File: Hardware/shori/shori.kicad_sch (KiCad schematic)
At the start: 100 parts, among them J1 430450200, J2 SWD_Header, J3 UART_Header, J4 530480310, J5 AudioJack3, J6 530480210, U1 CS4272, U2 STM32H750VBTx, U3 NE5532, U4 NE5532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

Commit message: Routing and memes done!!
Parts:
- removed J5: AudioJack3, Connector_Audio:Jack_3.5mm_CUI_SJ1-3523N_Horizontal, symbol Connector_Audio:AudioJack3
- removed U6: OPA134, Package_TO_SOT_SMD:SOT-23-5_HandSoldering, symbol Amplifier_Operational:OPA134
- added J5: Conn_01x03, Connector_JST:JST_PH_S3B-PH-K_1x03_P2.00mm_Horizontal, symbol Connector_Generic:Conn_01x03
- added J7: 530480210, My footprints:CONN02_530480210_MOL, symbol 2 Pin Audio Molex:530480210
- added U7: TLV9001IDCK, Package_TO_SOT_SMD:SOT-353_SC-70-5, symbol Amplifier_Operational:TLV9001IDCK
- H1, H2, H3, H4: footprint MountingHole:MountingHole_3mm -> MountingHole:MountingHole_3.5mm
- J1: footprint MyFootprints:CONN_SD-43045-001_02_MOL -> Connector_JST:JST_XH_S2B-XH-A_1x02_P2.50mm_Horizontal
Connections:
- net +5V: now also J7.2
- net +5VA: now also U7.5 (V+)
- net AUDIO_OUT: now also J6.1; no longer J6.2
- net GND: now also J6.2, J5.2 (Pin_2), J7.1, U7.2 (V-); no longer J6.1
- net JACKR: now also J5.1 (Pin_1)
- net JACKT: now also J5.3 (Pin_3)
- net SWCLK: now also J2.2 (Pin_2); no longer J2.3 (Pin_3)
- net SWDIO: now also J2.3 (Pin_3); no longer J2.2 (Pin_2)
- net at C43.1, C45.2, R28.2: now also U7.4
- net FEEDBACK_CAP: now reaches C45.1, R27.2
- net FEEDBACK_CAP: now also U7.3 (-)
- net at C44.1, R24.2: now also U7.1 (+)
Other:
- moved on the sheet: J4

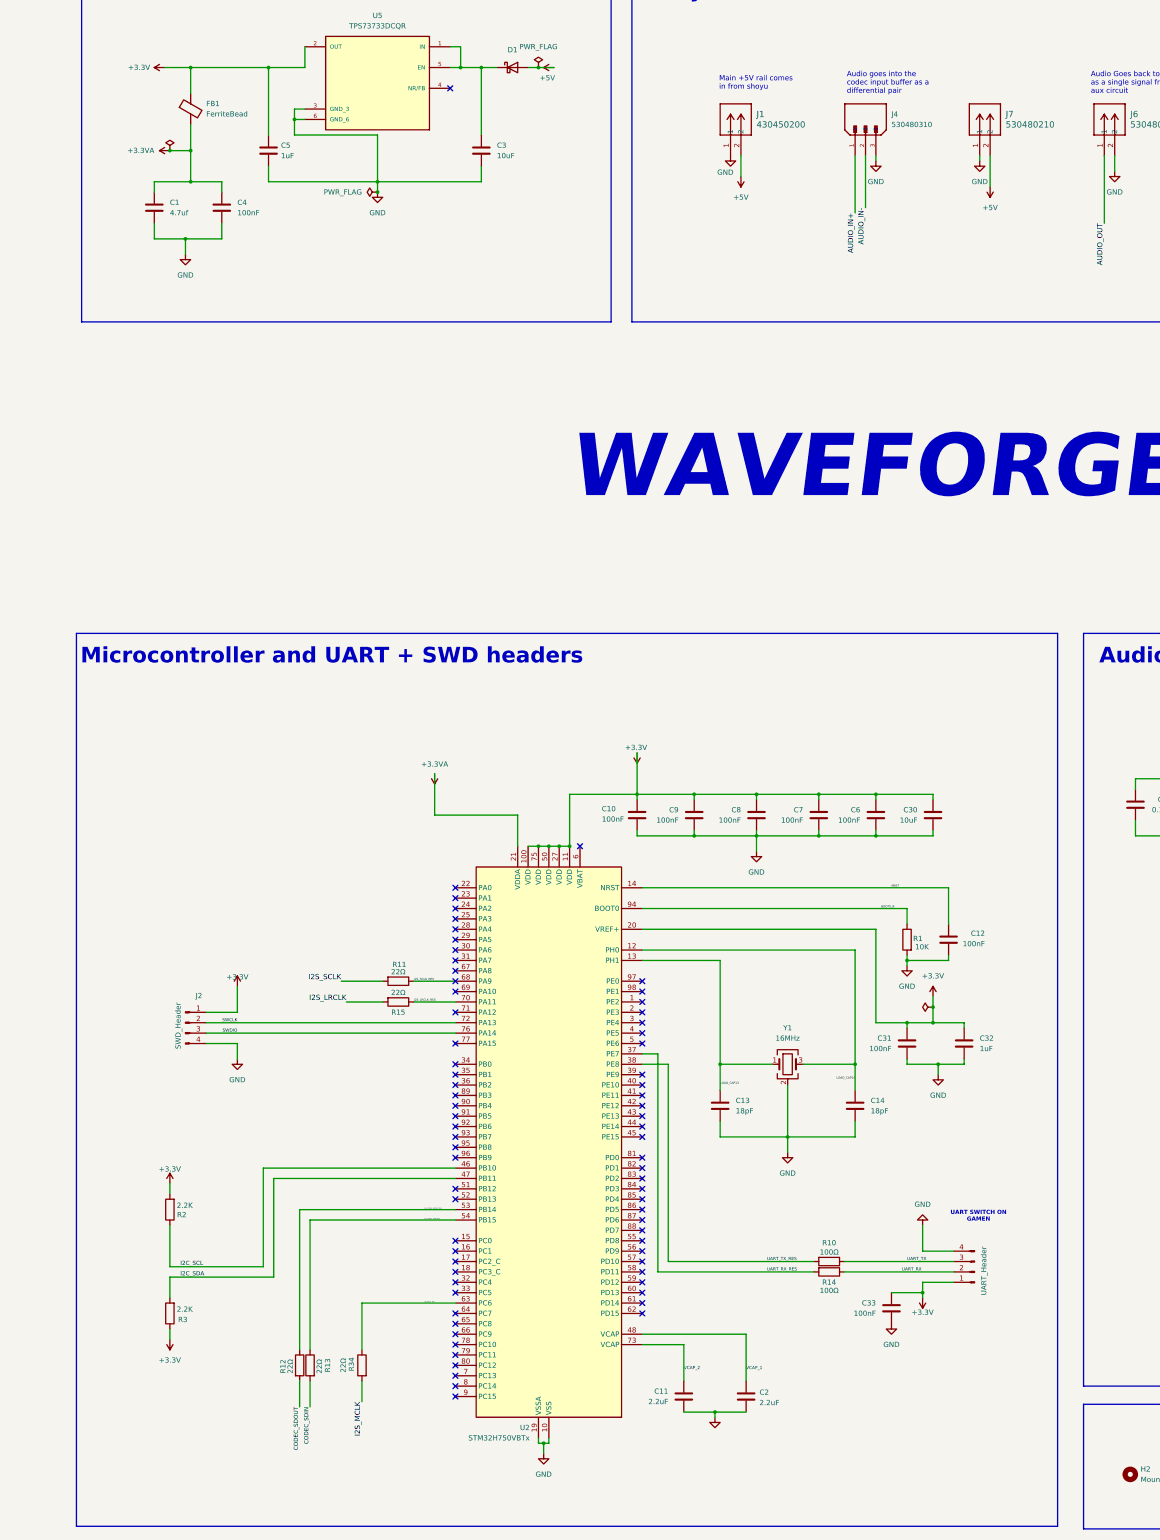
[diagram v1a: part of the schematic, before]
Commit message: Added flash sotrage, boot0 switch and nrst button in schems
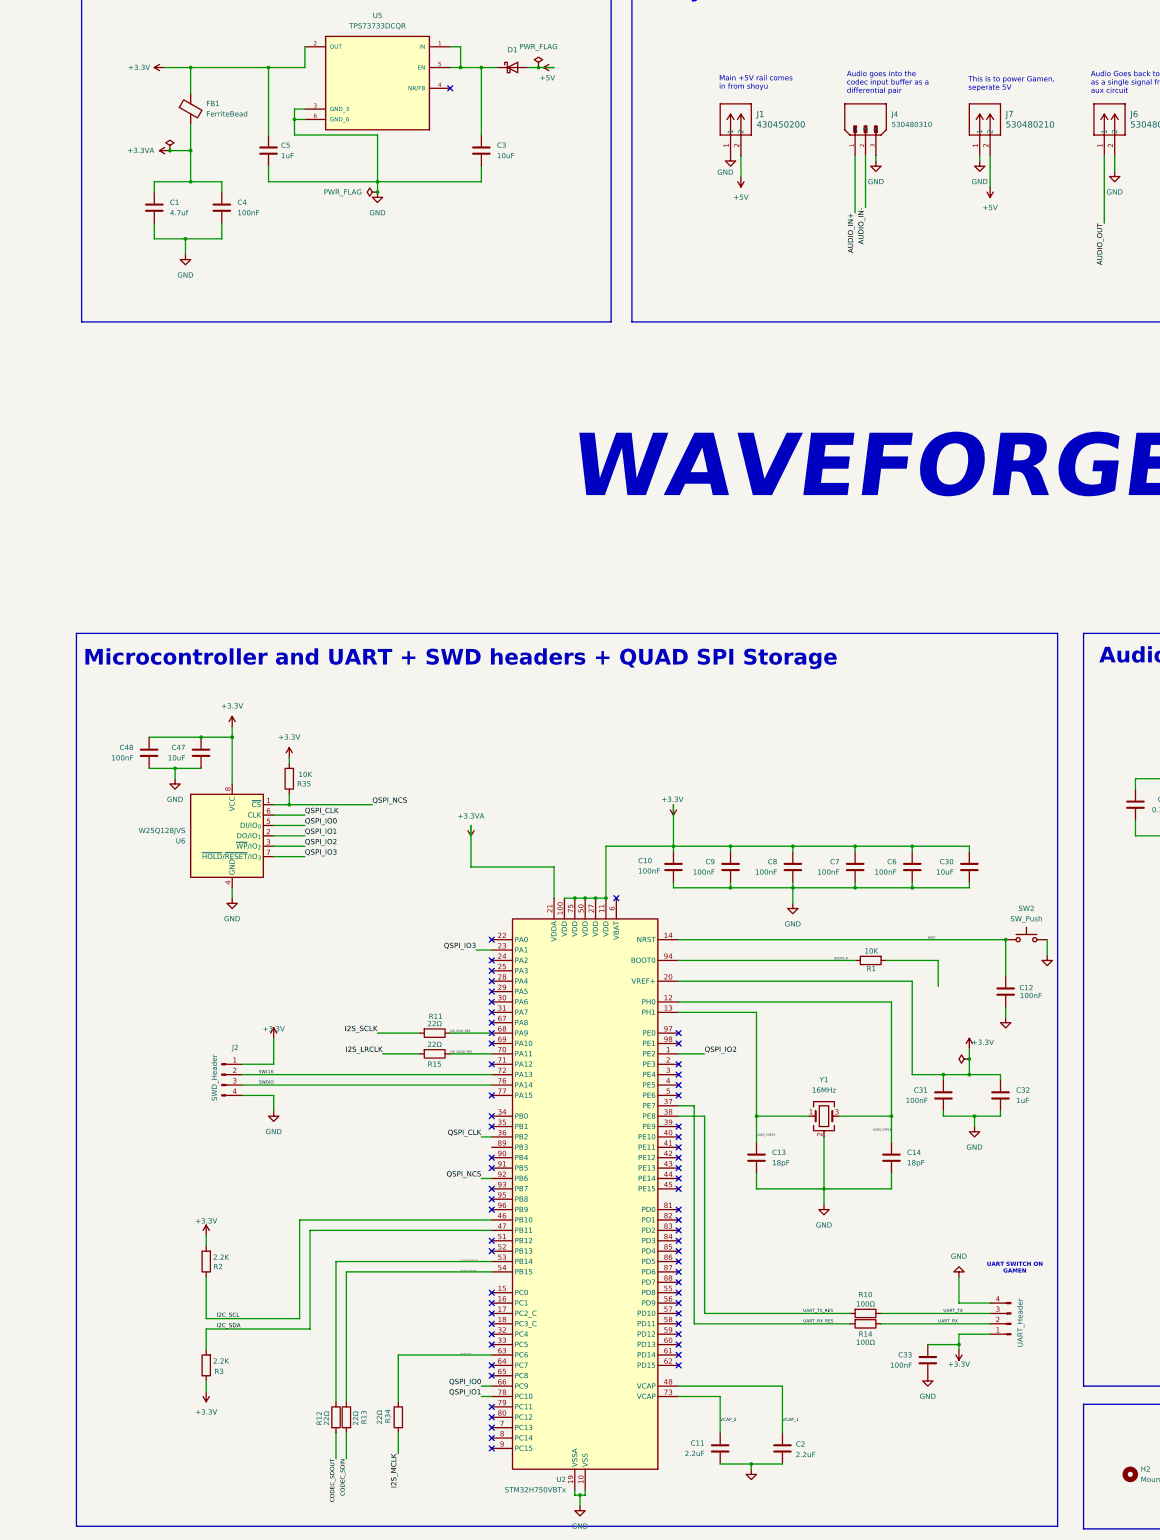
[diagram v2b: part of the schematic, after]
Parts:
- added C47: 10uF, Capacitor_SMD:C_0603_1608Metric_Pad1.08x0.95mm_HandSolder, symbol Device:C
- added C48: 100nF, Capacitor_SMD:C_0402_1005Metric_Pad0.74x0.62mm_HandSolder, symbol Device:C
- added R35: 10K, Resistor_SMD:R_0402_1005Metric_Pad0.72x0.64mm_HandSolder, symbol Device:R
- added SW2: SW_Push, symbol Switch:SW_Push
- added U6: W25Q128JVS, Package_SO:SOIC-8_5.3x5.3mm_P1.27mm, symbol Memory_Flash:W25Q128JVS
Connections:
- net +3.3V: now also C47.1, C48.1, R35.2, U6.8 (VCC)
- net GND: now also C47.2, C48.2, SW2.2, U6.4 (GND); no longer R1.2
- net NRST: now also SW2.1
- net QSPI_IO2: now reaches U2.1 (PE2)
- net QSPI_IO2: now also U6.3 (~{WP}/IO_{2})
- net QSPI_IO3: now reaches U2.23 (PA1)
- net QSPI_IO3: now also U6.7 (~{HOLD}/~{RESET}/IO_{3})
- net QSPI_CLK: now reaches U2.36 (PB2)
- net QSPI_CLK: now also U6.6 (CLK)
- net QSPI_IO0: now reaches U2.66 (PC9)
- net QSPI_IO0: now also U6.5 (DI/IO_{0})
- net QSPI_IO1: now reaches U2.78 (PC10)
- net QSPI_IO1: now also U6.2 (DO/IO_{1})
- net QSPI_NCS: now reaches U2.92 (PB6)
- net QSPI_NCS: now also R35.1, U6.1 (~{CS})
- no-connect marks 76 -> 69
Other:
- note added: "Microcontroller and UART + SWD headers + QUAD SPI Storage"
- note added: "This is to power Gamen, seperate 5V"
- note removed: "Microcontroller and UART + SWD headers"
- moved on the sheet: C10, C11, C12, C13, C14, C2, C30, C31, C32, C33, C6, C7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

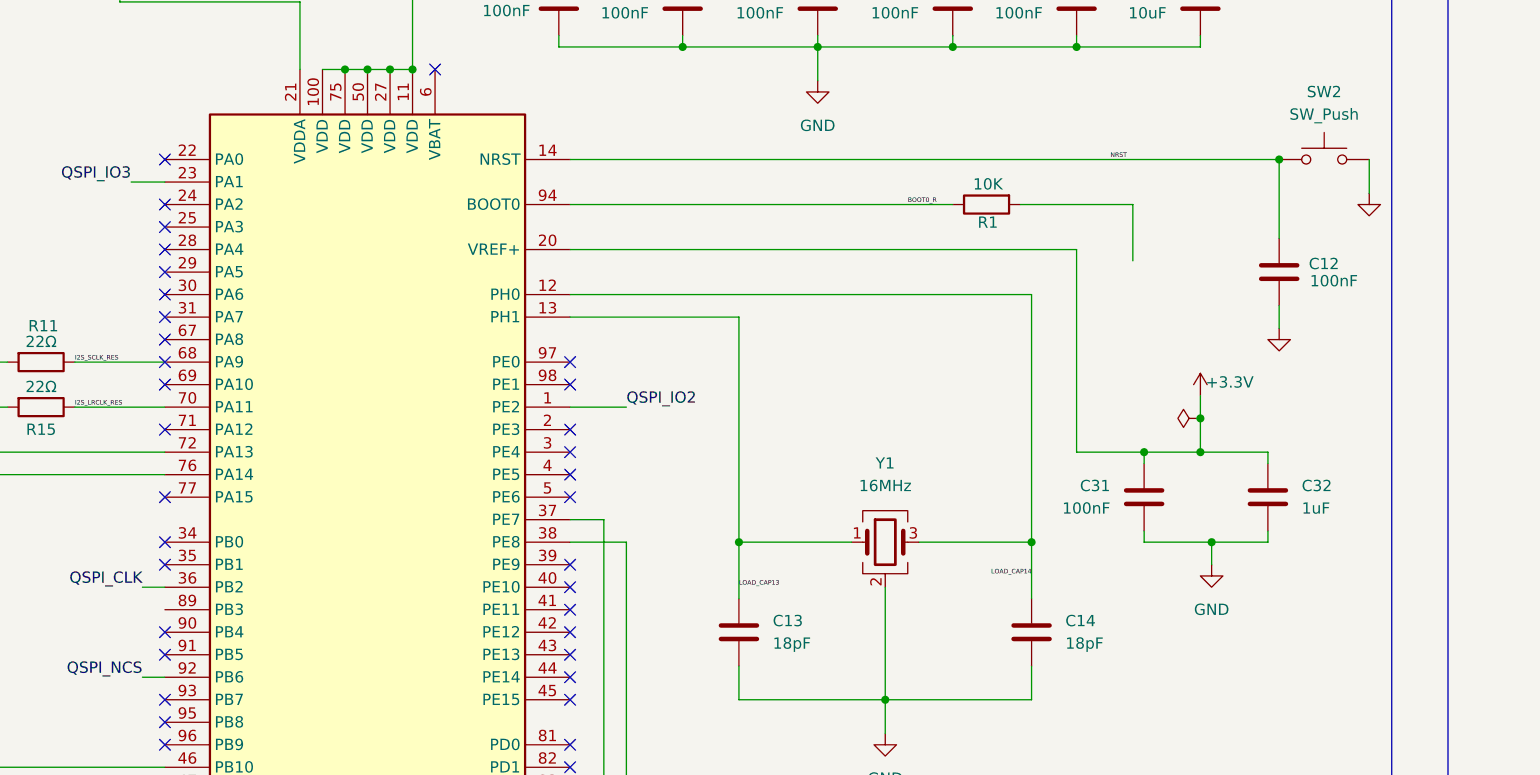
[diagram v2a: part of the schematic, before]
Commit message: Fixed Boot0 switch
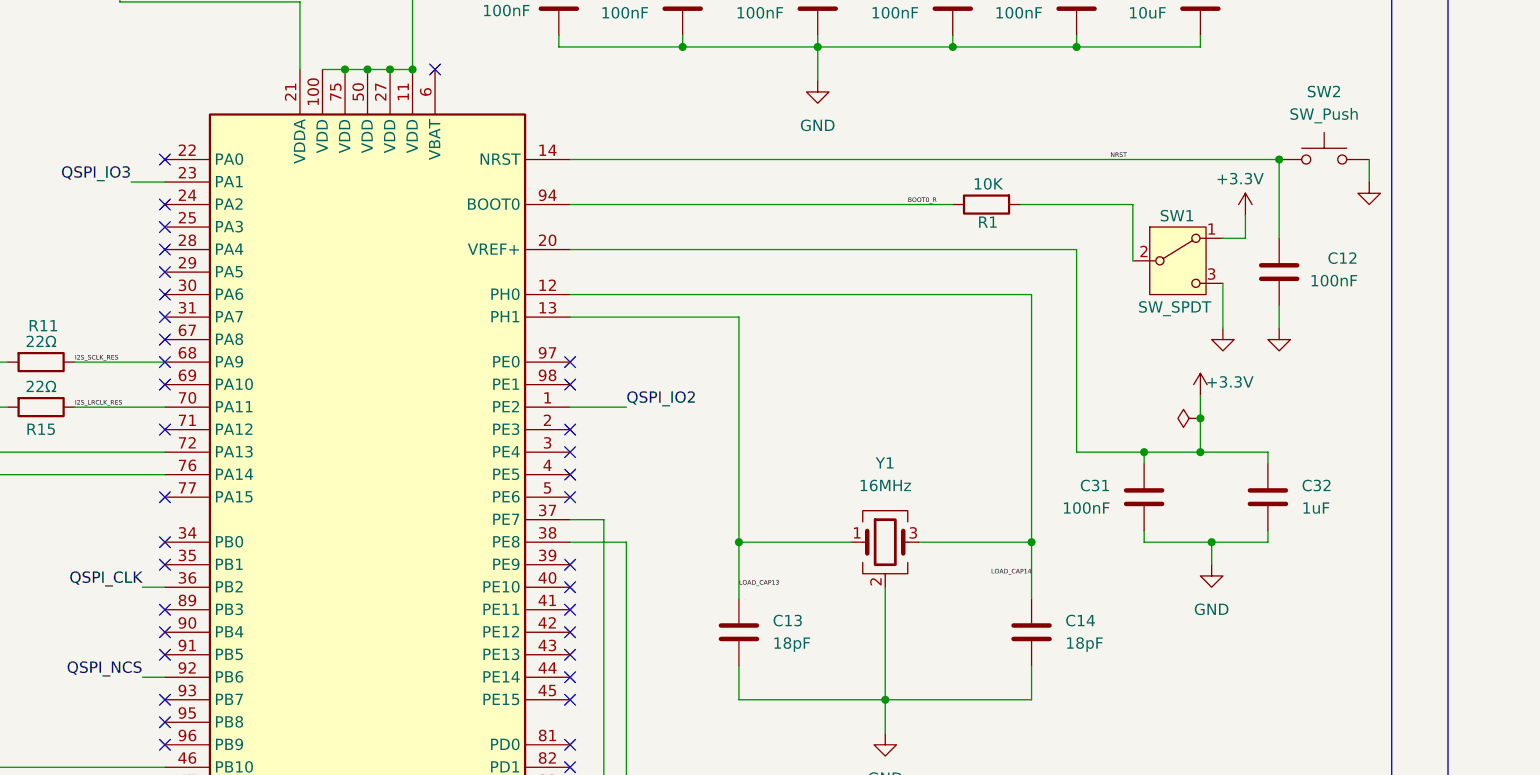
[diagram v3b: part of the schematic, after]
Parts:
- added SW1: SW_SPDT, symbol Switch:SW_SPDT
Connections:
- net +3.3V: now also SW1.1 (A)
- net GND: now also SW1.3 (C)
- net at R1.2: now also SW1.2 (B)
- no-connect marks 69 -> 70
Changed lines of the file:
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@@
 	)
 	(no_connect
+		(at 120.65 307.34)
+	)
+	(no_connect
 		(at 120.65 375.92)
 	)
@@
 	(wire
 		(pts
+			(xy 242.57 262.89) (xy 242.57 265.43)
+		)
+		(stroke
+			(width 0)
+			(type default)
+		)
+	)
+	(wire
+		(pts
 			(xy 57.15 207.01) (xy 57.15 218.44)
 		)
@@
 	(wire
 		(pts
+			(xy 256.54 256.54) (xy 256.54 259.08)
+		)
+		(stroke
+			(width 0)
+			(type default)
+		)
+	)
+	(wire
+		(pts
 			(xy 237.49 233.68) (xy 223.52 233.68)
 		)
@@
 	(wire
 		(pts
+			(xy 240.03 270.51) (xy 240.03 275.59)
+		)
+		(stroke
+			(width 0)
+			(type default)
+		)
+	)
+	(wire
+		(pts
 			(xy 551.18 256.54) (xy 542.29 256.54)
 		)
@@
 	(wire
 		(pts
-			(xy 406.4 290.83) (xy 406.4 306.07)
+			(xy 242.57 265.43) (xy 240.03 265.43)
 		)
 		(stroke
@@
 	(wire
 		(pts
-			(xy 408.94 66.04) (xy 408.94 73.66)
+			(xy 406.4 290.83) (xy 406.4 306.07)
 		)
 		(stroke
@@
 	(wire
 		(pts
-			(xy 542.29 300.99) (xy 552.45 300.99)
+			(xy 408.94 66.04) (xy 408.94 73.66)
 		)
 		(stroke
@@
 	(wire
 		(pts
-			(xy 434.34 53.34) (xy 431.8 53.34)
+			(xy 542.29 300.99) (xy 552.45 300.99)
 		)
 		(stroke
@@
 	(wire
 		(pts
-			(xy 194.31 243.84) (xy 194.31 247.65)
+			(xy 434.34 53.34) (xy 431.8 53.34)
 		)
 		(stroke
@@
 	(wire
 		(pts
-			(xy 256.54 256.54) (xy 256.54 260.35)
+			(xy 194.31 243.84) (xy 194.31 247.65)
 		)
 		(stroke
@@
 	)
 	(symbol
+		(lib_id "power:GND")
+		(at 240.03 275.59 0)
+		(mirror y)
+		(unit 1)
+		(exclude_from_sim no)
+		(in_bom yes)
+		(on_board yes)
+		(dnp no)
+		(property "Reference" "#PWR015"
+			(at 240.03 281.94 0)
+			(effects
+				(font
+					(size 1.27 1.27)
+				)
+				(hide yes)
+			)
+		)
+		(property "Value" "GND"
+			(at 236.5762 278.1754 0)
+			(effects
+				(font
+					(size 1.27 1.27)
+				)
+				(hide yes)
+			)
+		)
+		(property "Footprint" ""
+			(at 240.03 275.59 0)
+			(effects
+				(font
+					(size 1.27 1.27)
+				)
+				(hide yes)
+			)
+		)
+		(property "Datasheet" ""
+			(at 240.03 275.59 0)
+			(effects
+				(font
+					(size 1.27 1.27)
+				)
+				(hide yes)
+			)
+		)
+		(property "Description" "Power symbol creates a global label with name \"GND\" , ground"
+			(at 240.03 275.59 0)
+			(effects
+				(font
+					(size 1.27 1.27)
+				)
+				(hide yes)
+			)
+		)
+		(pin "1"
+		)
+		(instances
+			(project "shori"
+				(path "/bed06ac2-3d53-4627-b912-3f6150ebe2ee"
+					(reference "#PWR015")
+					(unit 1)
+				)
+			)
+		)
+	)
+	(symbol
 		(lib_id "Device:C")
 		(at 469.9 321.31 0)
@@
 	)
 	(symbol
-		(lib_id "power:GND")
-		(at 256.54 260.35 0)
-		(unit 1)
-		(exclude_from_sim no)
-		(in_bom yes)
-		(on_board yes)
-		(dnp no)
-		(property "Reference" "#PWR015"
-			(at 256.54 266.7 0)
-			(effects
-				(font
-					(size 1.27 1.27)
-				)
-				(hide yes)
-			)
-		)
-		(property "Value" "GND"
-			(at 259.9938 262.9354 0)
-			(effects
-				(font
-					(size 1.27 1.27)
-				)
-				(hide yes)
-			)
-		)
-		(property "Footprint" ""
-			(at 256.54 260.35 0)
-			(effects
-				(font
-					(size 1.27 1.27)
-				)
-				(hide yes)
-			)
-		)
-		(property "Datasheet" ""
-			(at 256.54 260.35 0)
-			(effects
-				(font
-					(size 1.27 1.27)
-				)
-				(hide yes)
-			)
-		)
-		(property "Description" "Power symbol creates a global label with name \"GND\" , ground"
-			(at 256.54 260.35 0)
-			(effects
-				(font
-					(size 1.27 1.27)
-				)
-				(hide yes)
-			)
-		)
-		(pin "1"
-		)
-		(instances
-			(project "shori"
-				(path "/bed06ac2-3d53-4627-b912-3f6150ebe2ee"
-					(reference "#PWR015")
-					(unit 1)
-				)
-			)
-		)
-	)
-	(symbol
 		(lib_id "Device:R")
 		(at 405.13 226.06 90)
@@
 		(dnp no)
 		(property "Reference" "C12"
-			(at 253.1521 268.3217 0)
+			(at 255.27 267.716 0)
 			(effects
 				(font
@@
 	)
 	(symbol
+		(lib_id "power:+3.3V")
+		(at 242.57 262.89 0)
+		(unit 1)
+		(exclude_from_sim no)
+		(in_bom yes)
+		(on_board yes)
+		(dnp no)
+		(property "Reference" "#PWR058"
+			(at 242.57 266.7 0)
+			(effects
+				(font
+					(size 1.27 1.27)
+				)
+				(hide yes)
+			)
+		)
+		(property "Value" "+3.3V"
+			(at 241.9494 258.7495 0)
+			(effects
+				(font
+					(size 1.27 1.27)
+				)
+			)
+		)
+		(property "Footprint" ""
+			(at 242.57 262.89 0)
+			(effects
+				(font
+					(size 1.27 1.27)
+				)
+				(hide yes)
+			)
+		)
+		(property "Datasheet" ""
+			(at 242.57 262.89 0)
+			(effects
+				(font
+					(size 1.27 1.27)
+				)
+				(hide yes)
+			)
+		)
+		(property "Description" "Power symbol creates a global label with name \"+3.3V\""
+			(at 242.57 262.89 0)
+			(effects
+				(font
+					(size 1.27 1.27)
+				)
+				(hide yes)
+			)
+		)
+		(pin "1"
+		)
+		(instances
+			(project ""
+				(path "/bed06ac2-3d53-4627-b912-3f6150ebe2ee"
+					(reference "#PWR058")
+					(unit 1)
+				)
+			)
+		)
+	)
+	(symbol
 		(lib_id "power:GND")
 		(at 469.9 325.12 0)
@@
 	)
 	(symbol
+		(lib_id "Switch:SW_SPDT")
+		(at 234.95 267.97 0)
+		(unit 1)
+		(exclude_from_sim no)
+		(in_bom yes)
+		(on_board yes)
+		(dnp no)
+		(property "Reference" "SW1"
+			(at 234.8669 262.9248 0)
+			(effects
+				(font
+					(size 1.27 1.27)
+				)
+			)
+		)
+		(property "Value" "SW_SPDT"
+			(at 234.5886 273.2238 0)
+			(effects
+				(font
+					(size 1.27 1.27)
+				)
+			)
+		)
+		(property "Footprint" ""
+			(at 234.95 267.97 0)
+			(effects
+				(font
+					(size 1.27 1.27)
+				)
+				(hide yes)
+			)
+		)
+		(property "Datasheet" "~"
+			(at 234.95 275.59 0)
+			(effects
+				(font
+					(size 1.27 1.27)
+				)
+				(hide yes)
+			)
+		)
+		(property "Description" "Switch, single pole double throw"
+			(at 234.95 267.97 0)
+			(effects
+				(font
+					(size 1.27 1.27)
+				)
+				(hide yes)
+			)
+		)
+		(pin "1"
+		)
+		(pin "3"
+		)
+		(pin "2"
+		)
+		(instances
+			(project ""
+				(path "/bed06ac2-3d53-4627-b912-3f6150ebe2ee"
+					(reference "SW1")
+					(unit 1)
+				)
+			)
+		)
+	)
+	(symbol
 		(lib_id "Amplifier_Operational:TLV9001IDCK")
 		(at 447.04 228.6 0)
@@
 					(unit 1)
 				)
+			)
+		)
+	)
+	(symbol
+		(lib_id "power:GND")
+		(at 256.54 259.08 0)
+		(unit 1)
+		(exclude_from_sim no)
+		(in_bom yes)
+		(on_board yes)
+		(dnp no)
+		(property "Reference" "#PWR060"
+			(at 256.54 265.43 0)
+			(effects
+				(font
+					(size 1.27 1.27)
+				)
+				(hide yes)
+			)
+		)
+		(property "Value" "GND"
+			(at 259.9938 261.6654 0)
+			(effects
+				(font
+					(size 1.27 1.27)
+				)
+				(hide yes)
+			)
+		)
+		(property "Footprint" ""
+			(at 256.54 259.08 0)
+			(effects
+				(font
+					(size 1.27 1.27)
+				)
+				(hide yes)
+			)
+		)
+		(property "Datasheet" ""
+			(at 256.54 259.08 0)
+			(effects
+				(font
+					(size 1.27 1.27)
+				)
+				(hide yes)
+			)
+		)
+		(property "Description" "Power symbol creates a global label with name \"GND\" , ground"
+			(at 256.54 259.08 0)
+			(effects
+				(font
+					(size 1.27 1.27)
+				)
+				(hide yes)
+			)
+		)
+		(pin "1"
+		)
+		(instances
+			(project "shori"
+				(path "/bed06ac2-3d53-4627-b912-3f6150ebe2ee"
+					(reference "#PWR060")
+					(unit 1)
+				)
